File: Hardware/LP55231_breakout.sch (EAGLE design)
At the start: 29 parts, among them J1 To micro, J2 USER LED, J3 USER LED, J4 USER LED, U1 LP55231WQFN

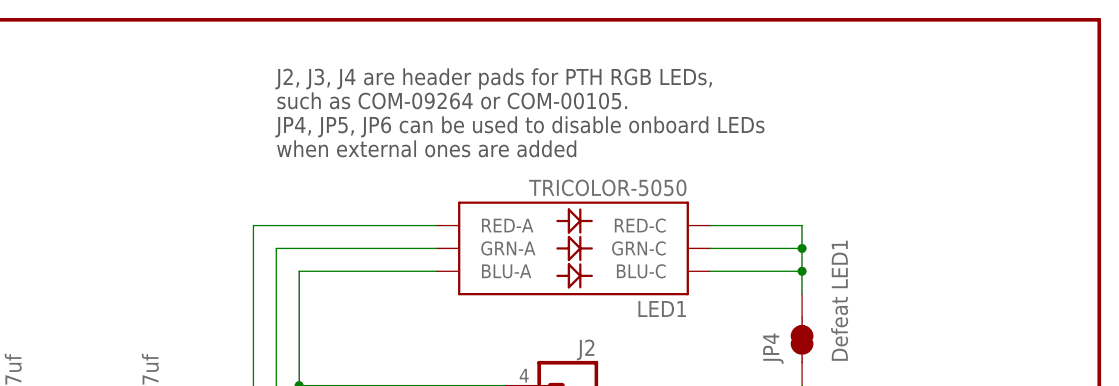
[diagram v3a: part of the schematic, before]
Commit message: Clarifying one schematic note.
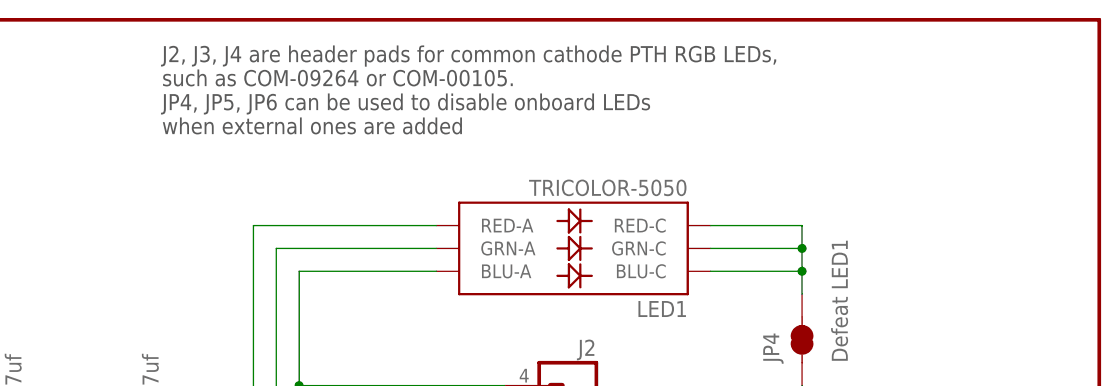
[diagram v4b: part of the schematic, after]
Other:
- note added: "J2, J3, J4 are header pads for common cathode PTH RGB LEDs, such as COM-09264 or COM-00105. JP4, JP5, JP6 can be used to disable onboard LEDs when external ones are added"
- note removed: "J2, J3, J4 are header pads for PTH RGB LEDs, such as COM-09264 or COM-00105. JP4, JP5, JP6 can be used to disable onboard LEDs when external ones are added"
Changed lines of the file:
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@@
 1,0 - 0x34
 1,1 - 0x35</text>
-<text x="157.48" y="170.18" size="1.778" layer="97" font="vector">J2, J3, J4 are header pads for PTH RGB LEDs,
+<text x="144.78" y="172.72" size="1.778" layer="97" font="vector">J2, J3, J4 are header pads for common cathode PTH RGB LEDs,
 such as COM-09264 or COM-00105.
 JP4, JP5, JP6 can be used to disable onboard LEDs

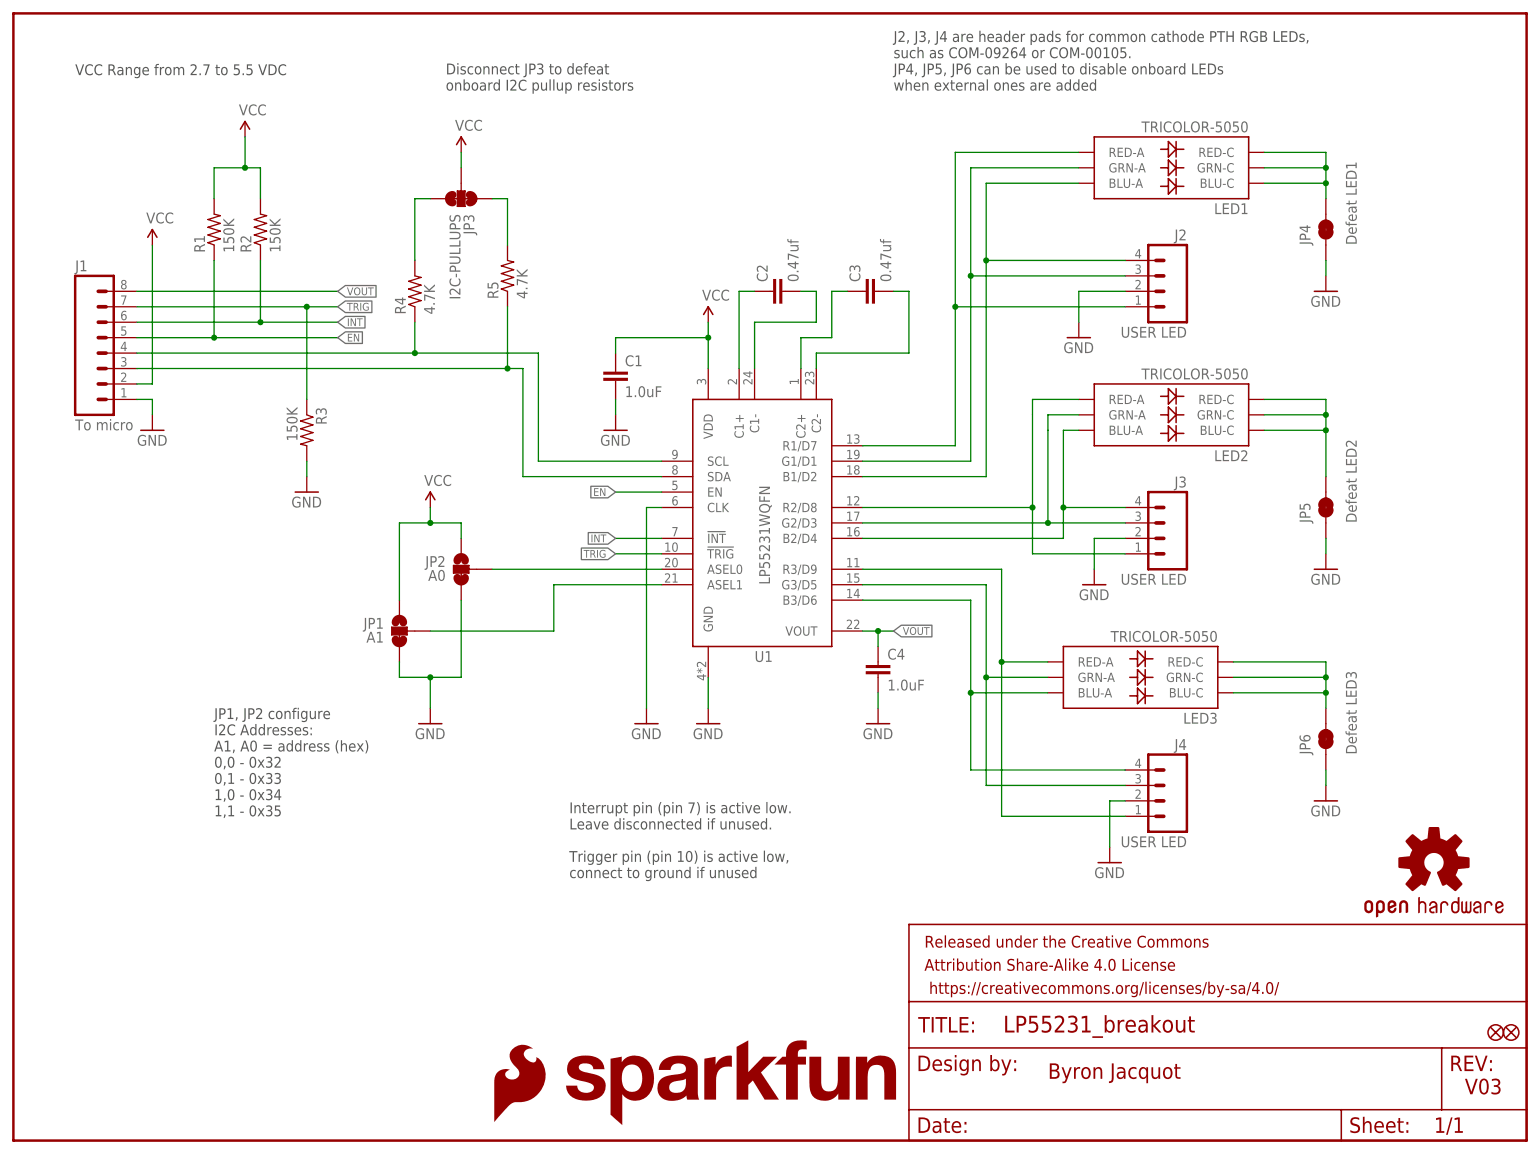
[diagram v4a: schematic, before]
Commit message: Making updates after group & checklist reviews.
Rolling version # to V10.
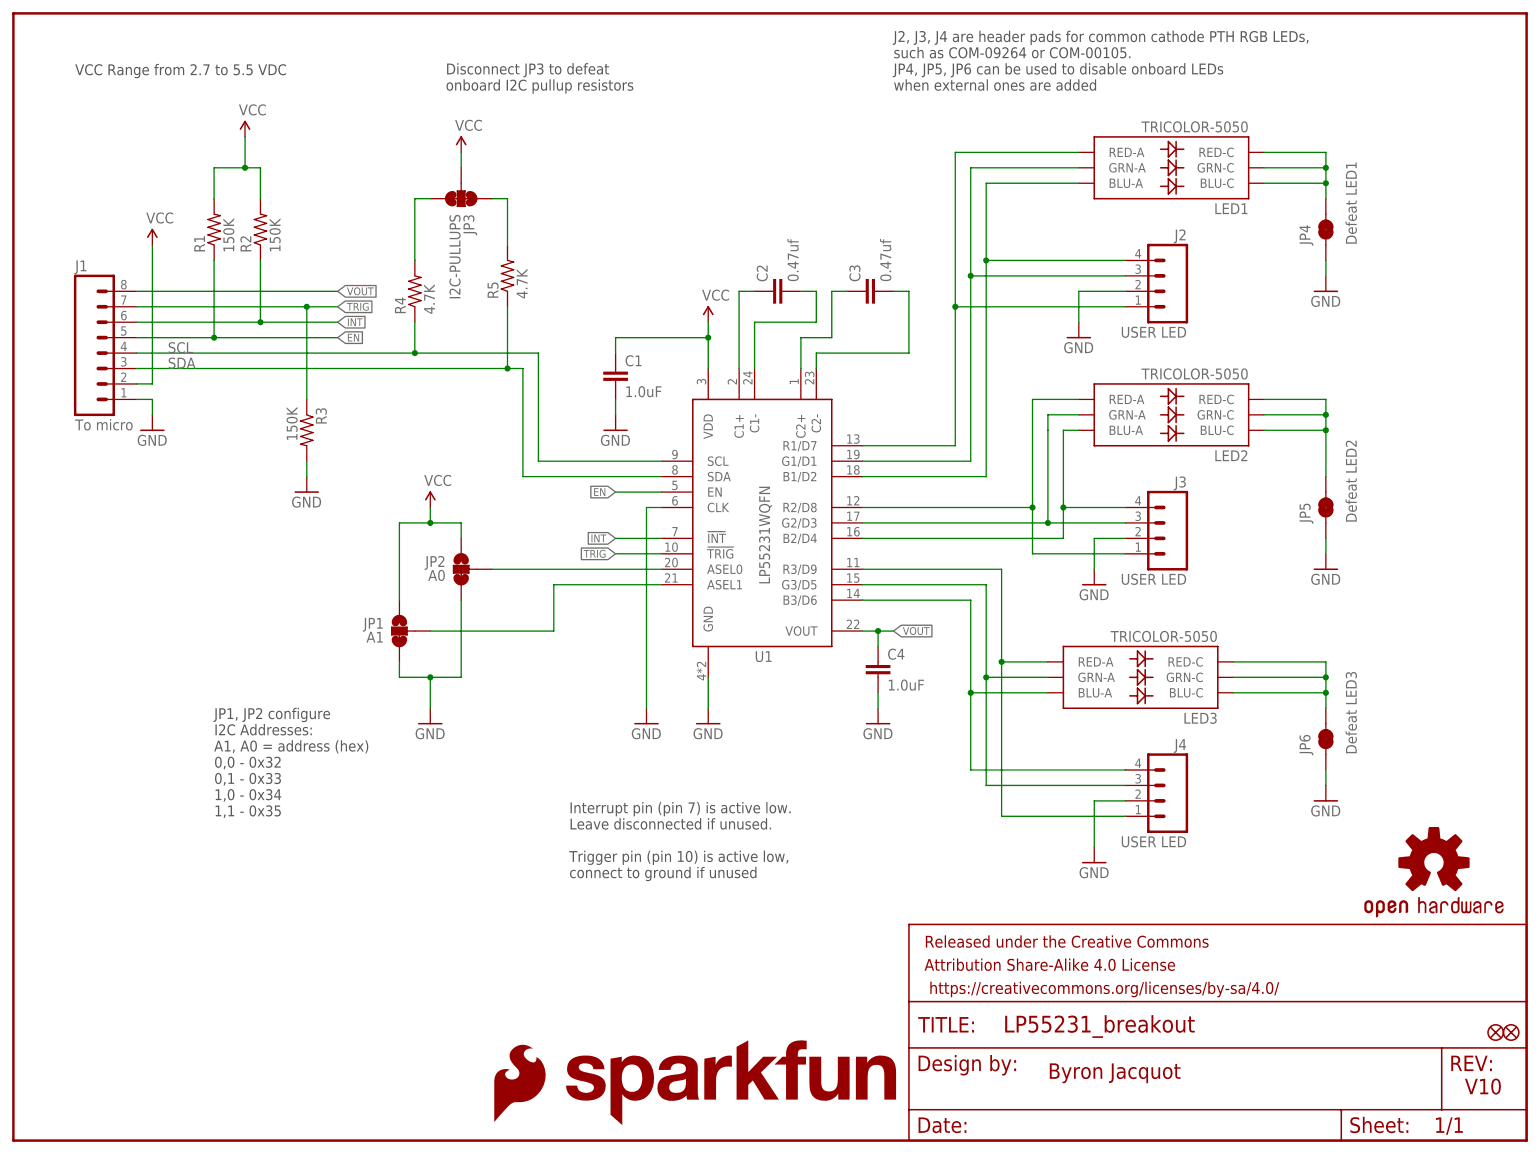
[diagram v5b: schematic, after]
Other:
- note added: "V10"
- note removed: "V03"
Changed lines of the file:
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@@
 <drawing>
 <settings>
-<setting alwaysvectorfont="no"/>
+<setting alwaysvectorfont="yes"/>
 <setting verticaltext="up"/>
 </settings>
@@
 <plain>
 <text x="170.18" y="10.16" size="2.54" layer="94" font="vector">Byron Jacquot</text>
-<text x="238.76" y="7.62" size="2.54" layer="94" font="vector">V03</text>
+<text x="238.76" y="7.62" size="2.54" layer="94" font="vector">V10</text>
 <text x="10.16" y="175.26" size="1.778" layer="97" font="vector">VCC Range from 2.7 to 5.5 VDC</text>
 <text x="33.02" y="53.34" size="1.778" layer="97" font="vector">JP1, JP2 configure
@@
 <instance part="J3" gate="G$1" x="187.96" y="99.06" rot="MR0"/>
 <instance part="J4" gate="G$1" x="187.96" y="55.88" rot="MR0"/>
-<instance part="GND10" gate="1" x="180.34" y="45.72"/>
+<instance part="GND10" gate="1" x="177.8" y="45.72"/>
 <instance part="GND9" gate="1" x="177.8" y="91.44"/>
 <instance part="GND8" gate="1" x="175.26" y="132.08"/>
@@
 <segment>
 <pinref part="GND10" gate="1" pin="GND"/>
-<wire x1="180.34" y1="48.26" x2="180.34" y2="55.88" width="0.1524" layer="91"/>
+<wire x1="177.8" y1="48.26" x2="177.8" y2="55.88" width="0.1524" layer="91"/>
 <pinref part="J4" gate="G$1" pin="2"/>
-<wire x1="180.34" y1="55.88" x2="182.88" y2="55.88" width="0.1524" layer="91"/>
+<wire x1="177.8" y1="55.88" x2="182.88" y2="55.88" width="0.1524" layer="91"/>
 </segment>
 <segment>
@@
 <junction x="66.04" y="129.54"/>
 <pinref part="J1" gate="G$1" pin="4"/>
+<label x="25.4" y="129.54" size="1.778" layer="95" font="vector"/>
 </segment>
 </net>
@@
 <pinref part="U1" gate="G$1" pin="EN"/>
 <wire x1="106.68" y1="106.68" x2="99.06" y2="106.68" width="0.1524" layer="91"/>
-<label x="99.06" y="106.68" size="1.27" layer="95" rot="R180" xref="yes"/>
+<label x="99.06" y="106.68" size="1.27" layer="95" font="vector" rot="R180" xref="yes"/>
 </segment>
 <segment>
 <wire x1="20.32" y1="132.08" x2="33.02" y2="132.08" width="0.1524" layer="91"/>
-<label x="53.34" y="132.08" size="1.27" layer="95" xref="yes"/>
+<label x="53.34" y="132.08" size="1.27" layer="95" font="vector" xref="yes"/>
 <pinref part="J1" gate="G$1" pin="5"/>
 <pinref part="R1" gate="G$1" pin="1"/>
@@
 <junction x="81.28" y="127"/>
 <pinref part="J1" gate="G$1" pin="3"/>
+<label x="25.4" y="127" size="1.778" layer="95" font="vector"/>
 </segment>
 </net>
@@
 <pinref part="U1" gate="G$1" pin="!INT"/>
 <wire x1="106.68" y1="99.06" x2="99.06" y2="99.06" width="0.1524" layer="91"/>
-<label x="99.06" y="99.06" size="1.27" layer="95" rot="R180" xref="yes"/>
+<label x="99.06" y="99.06" size="1.27" layer="95" font="vector" rot="R180" xref="yes"/>
 </segment>
 <segment>
 <wire x1="20.32" y1="134.62" x2="40.64" y2="134.62" width="0.1524" layer="91"/>
-<label x="53.34" y="134.62" size="1.27" layer="95" xref="yes"/>
+<label x="53.34" y="134.62" size="1.27" layer="95" font="vector" xref="yes"/>
 <pinref part="J1" gate="G$1" pin="6"/>
 <pinref part="R2" gate="G$1" pin="1"/>
@@
 <pinref part="U1" gate="G$1" pin="!TRIG"/>
 <wire x1="106.68" y1="96.52" x2="99.06" y2="96.52" width="0.1524" layer="91"/>
-<label x="99.06" y="96.52" size="1.27" layer="95" rot="R180" xref="yes"/>
+<label x="99.06" y="96.52" size="1.27" layer="95" font="vector" rot="R180" xref="yes"/>
 </segment>
 <segment>
 <wire x1="20.32" y1="137.16" x2="48.26" y2="137.16" width="0.1524" layer="91"/>
-<label x="53.34" y="137.16" size="1.27" layer="95" xref="yes"/>
+<label x="53.34" y="137.16" size="1.27" layer="95" font="vector" xref="yes"/>
 <pinref part="J1" gate="G$1" pin="7"/>
 <pinref part="R3" gate="G$1" pin="1"/>
